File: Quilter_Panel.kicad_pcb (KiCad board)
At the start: 2 copper layers, 40.4 x 128.5 mm, 15 parts

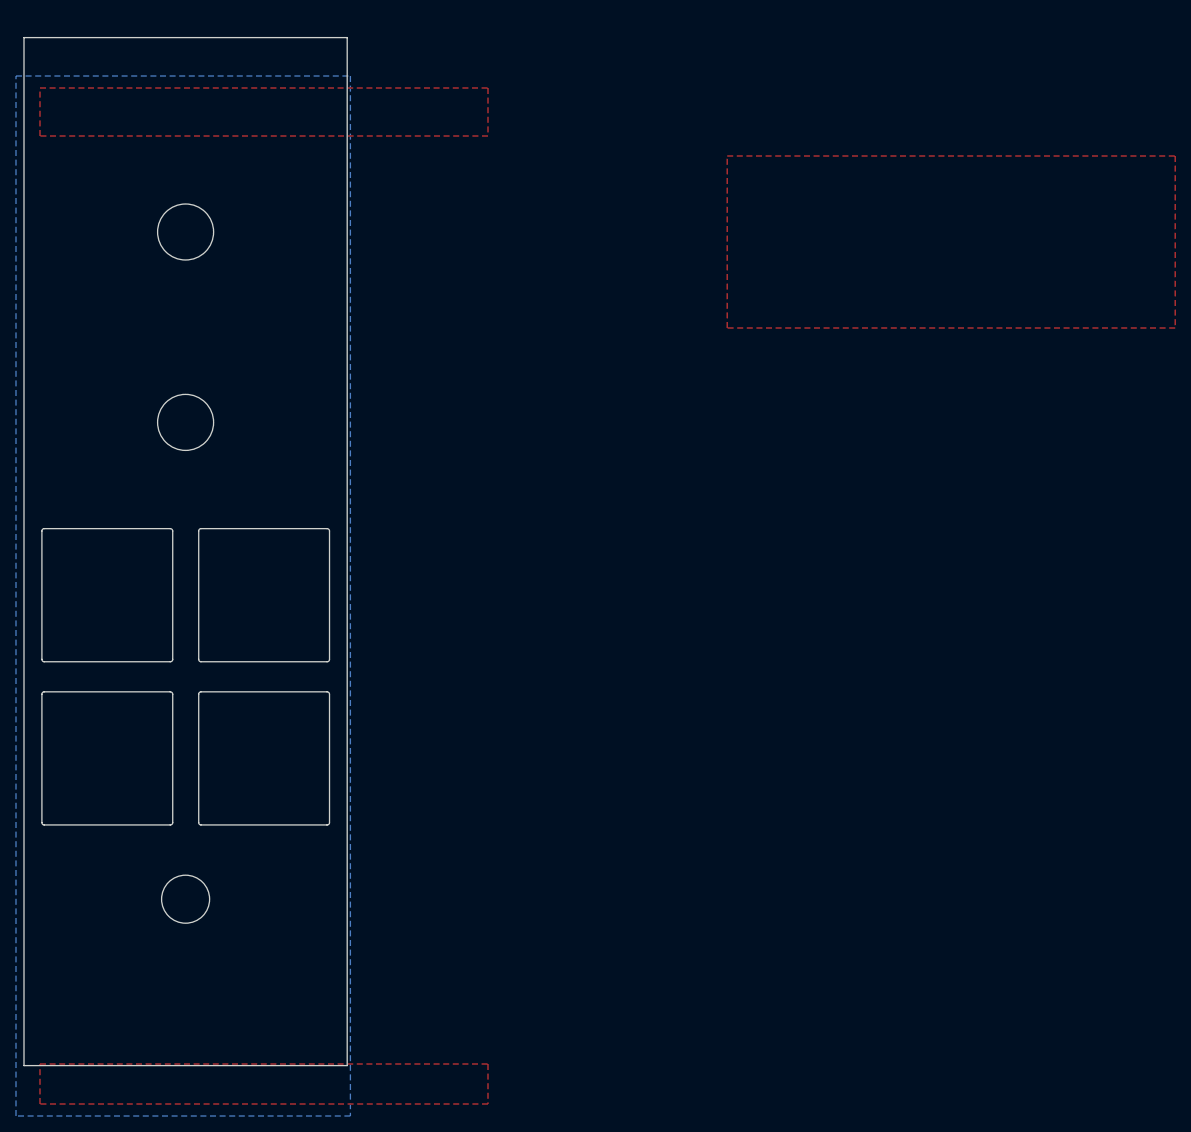
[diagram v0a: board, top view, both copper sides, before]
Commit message: Added all voice filter CV; panel draft done
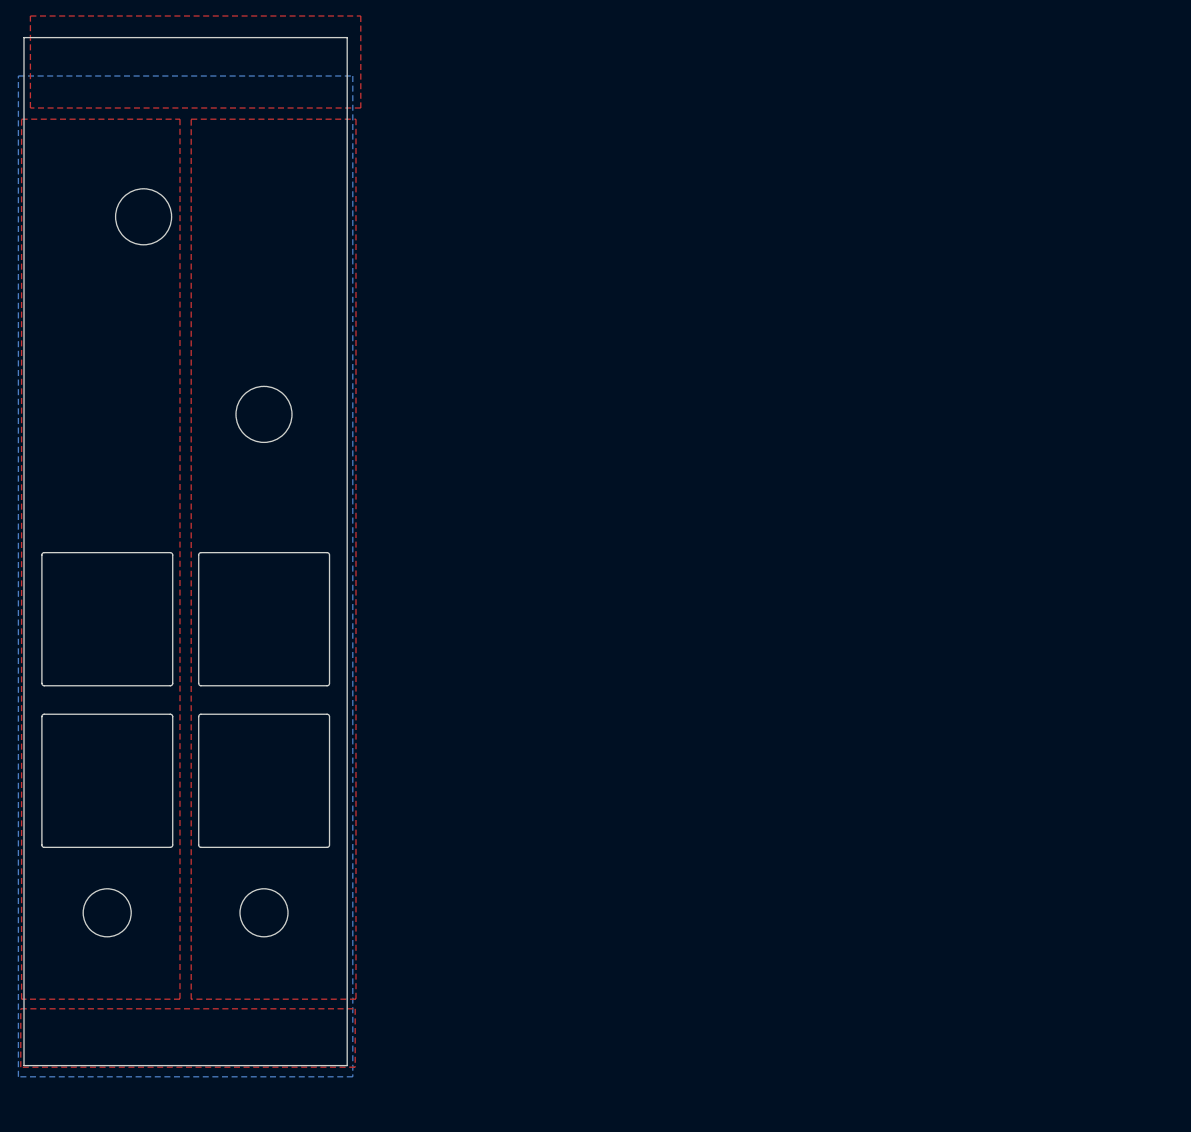
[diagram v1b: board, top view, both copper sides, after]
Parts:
- removed the Ref** at (82.9, 34.2)
- removed the Ref** at (57.5, 156.7)
- removed kibuzzard-63D12809: G***, kibuzzard-63D12809
- removed kibuzzard-63D139E5: G***, kibuzzard-63D139E5
- removed kibuzzard-63D2A377: G***, kibuzzard-63D2A377
- removed kibuzzard-63D2A3C5: G***, kibuzzard-63D2A3C5
- added G***: LOGO, Graphics:Quilter, F.Cu at (75.2, 34.9)
- added Ref**: Thonkiconn_Socket_MountingHole_6mm, Custom_Footprints:Thonkiconn_Socket_MountingHole_6mm, F.Cu at (60.4, 140.6)
- added kibuzzard-63FA2F5E: G***, kibuzzard-63FA2F5E, F.Cu at (85.6, 89.0)
- added kibuzzard-63FBA07E: G***, kibuzzard-63FBA07E, F.Cu at (56.1, 147.9)
- added kibuzzard-63FBA3C4: G***, kibuzzard-63FBA3C4, F.Cu at (60.4, 84.6)
- added kibuzzard-63FBA5D0: G***, kibuzzard-63FBA5D0, F.Cu at (84.1, 148.0)
- added kibuzzard-63FBA61E: G***, kibuzzard-63FBA61E, F.Cu at (80.1, 58.7)
- moved Ref** 9.95 mm to (80.0, 140.6)
- moved Ref** 9.85 mm to (80.0, 78.3)
- moved Ref** 5.58 mm to (65.0, 53.6)
- moved FM_In 3.00 mm to (60.4, 103.9)
- moved PWM_In 3.00 mm to (80.0, 103.9)
- moved Output 2.80 mm to (80.0, 124.1)
- moved V_per_Oct_In 2.80 mm to (60.4, 124.1)

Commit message: Updates to panel and component boards
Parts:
- removed kibuzzard-63FA2F5E: G***, kibuzzard-63FA2F5E
- removed kibuzzard-63FBA61E: G***, kibuzzard-63FBA61E
- added kibuzzard-63FBCCA9: G***, kibuzzard-63FBCCA9, F.Cu at (84.3, 89.0)
- added kibuzzard-63FBD1AD: G***, kibuzzard-63FBD1AD, F.Cu at (80.1, 55.6)
- moved Ref** 1.70 mm to (80.0, 76.6)
- moved kibuzzard-63FBA5D0 0.05 mm to (84.2, 148.0)

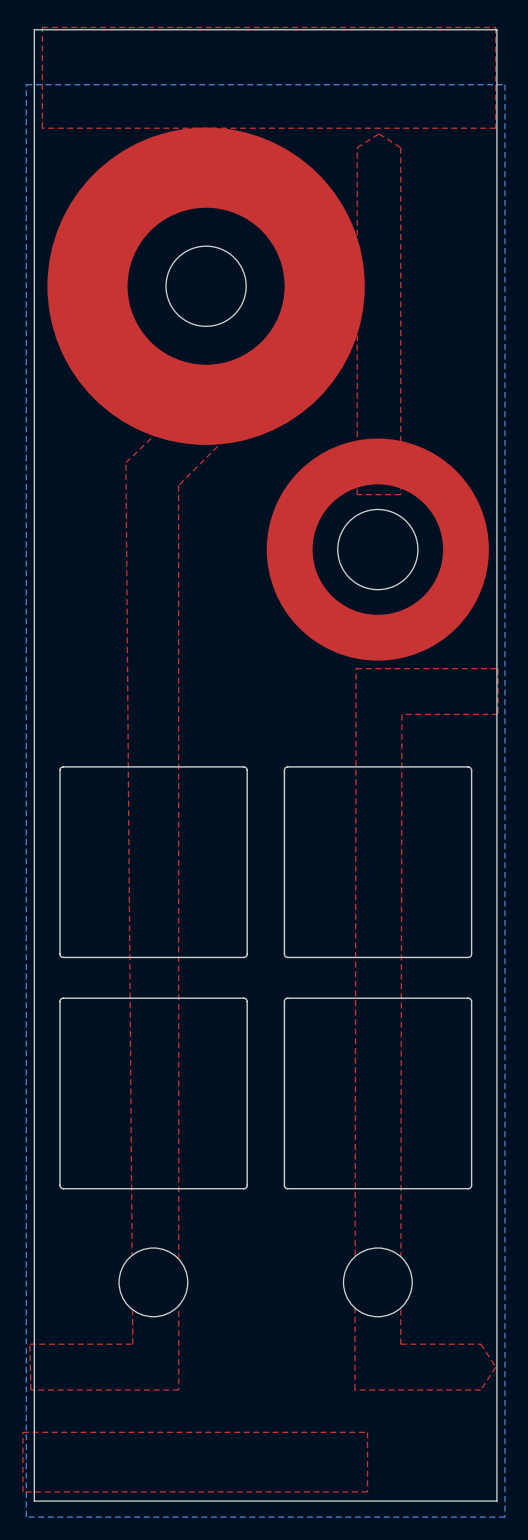
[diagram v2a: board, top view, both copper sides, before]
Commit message: Cleaned up panel and PCBs
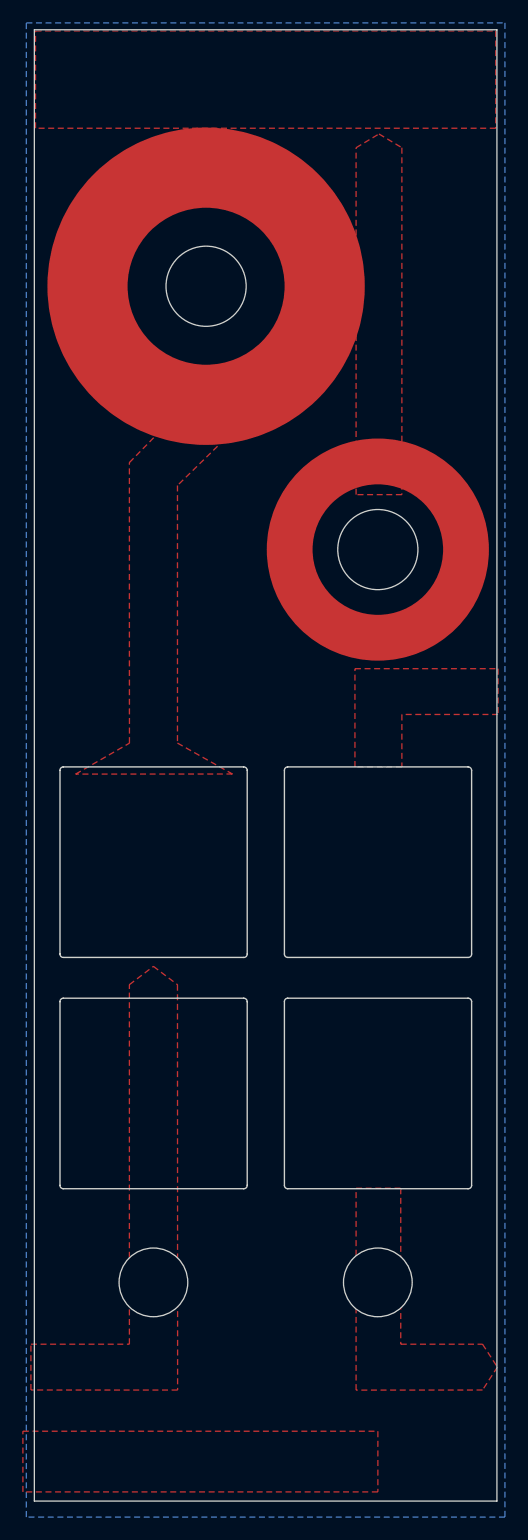
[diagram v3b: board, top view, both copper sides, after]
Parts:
- removed kibuzzard-63FBA3C4: G***, kibuzzard-63FBA3C4
- added kibuzzard-6400749B: G***, kibuzzard-6400749B, F.Cu at (60.4, 82.0)
